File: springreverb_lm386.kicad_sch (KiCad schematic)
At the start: 67 parts, among them J1 IN, J10 VR2_3, J11 VR_2_2, J12 VR_2GND, J13 To, J14 FromSW, J15 To_Tank, J16 From_Tank, J17 FromGND, J18 From, J19 VR3_3, J2 INGND, J20 VR_4_3, J21 VR4_1, J22 OUT, J3 GND, J4 Vin, J5 LEDGND, J6 VR1_3, J7 toC6, J8 toC7, J9 FromC, SW1 SW_SPDT, SW2 SW_SPST, U1 TL072, U2 TC1044S, U3 LM386

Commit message: 接続の名称を変更
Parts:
- J9: value FromC -> FromC1
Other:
- moved on the sheet: J9
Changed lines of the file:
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@@
+	)
+	(junction
+		(at 39.37 140.97)
+		(diameter 0)
+		(color 0 0 0 0)
 	)
 	(junction
@@
 	)
 	(junction
-		(at 97.79 162.56)
-		(diameter 0)
-		(color 0 0 0 0)
-	)
-	(junction
 		(at 58.42 68.58)
 		(diameter 0)
@@
 	(wire
 		(pts
-			(xy 71.12 162.56) (xy 97.79 162.56)
+			(xy 71.12 162.56) (xy 105.41 162.56)
 		)
 		(stroke
@@
 	(wire
 		(pts
+			(xy 39.37 140.97) (xy 43.18 140.97)
+		)
+		(stroke
+			(width 0)
+			(type default)
+		)
+	)
+	(wire
+		(pts
 			(xy 60.96 68.58) (xy 58.42 68.58)
 		)
@@
 	(wire
 		(pts
-			(xy 26.67 140.97) (xy 43.18 140.97)
+			(xy 26.67 140.97) (xy 39.37 140.97)
 		)
 		(stroke
@@
 		(pts
 			(xy 165.1 143.51) (xy 165.1 144.78)
-		)
-		(stroke
-			(width 0)
-			(type default)
-		)
-	)
-	(wire
-		(pts
-			(xy 97.79 162.56) (xy 105.41 162.56)
 		)
 		(stroke
@@
 	(symbol
 		(lib_id "Connector:Conn_01x01_Pin")
-		(at 97.79 157.48 270)
+		(at 39.37 146.05 90)
 		(unit 1)
 		(body_style 1)
@@
 		(in_pos_files yes)
 		(dnp no)
-		(fields_autoplaced yes)
 		(property "Reference" "J9"
-			(at 99.06 156.8449 90)
+			(at 38.1 146.6851 90)
 			(show_name no)
 			(do_not_autoplace no)
@@
 			)
 		)
-		(property "Value" "FromC"
-			(at 99.06 159.3849 90)
+		(property "Value" "FromC1"
+			(at 38.1 144.272 90)
 			(show_name no)
 			(do_not_autoplace no)
@@
 		)
 		(property "Footprint" "MyLibrary:PinHeader_1x01_P2.54mm_Vertical"
-			(at 97.79 157.48 0)
+			(at 39.37 146.05 0)
 			(hide yes)
 			(show_name no)
@@
 		)
 		(property "Datasheet" ""
-			(at 97.79 157.48 0)
+			(at 39.37 146.05 0)
 			(hide yes)
 			(show_name no)
@@
 		)
 		(property "Description" "Generic connector, single row, 01x01, script generated"
-			(at 97.79 157.48 0)
+			(at 39.37 146.05 0)
 			(hide yes)
 			(show_name no)

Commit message: 不要な配線を修正
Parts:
- removed J12: VR_2GND, MyLibrary:PinHeader_1x01_P2.54mm_Vertical, symbol Connector:Conn_01x01_Pin
- J9: value FromC1 -> VR_1_1
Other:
- moved on the sheet: J9
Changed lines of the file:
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@@
-	)
-	(junction
-		(at 39.37 140.97)
-		(diameter 0)
-		(color 0 0 0 0)
 	)
 	(junction
@@
 	)
 	(junction
-		(at 124.46 162.56)
-		(diameter 0)
-		(color 0 0 0 0)
-	)
-	(junction
 		(at 166.37 34.29)
 		(diameter 0)
@@
 	)
 	(junction
+		(at 76.2 162.56)
+		(diameter 0)
+		(color 0 0 0 0)
+	)
+	(junction
 		(at 58.42 91.44)
 		(diameter 0)
@@
 	(wire
 		(pts
+			(xy 76.2 162.56) (xy 105.41 162.56)
+		)
+		(stroke
+			(width 0)
+			(type default)
+		)
+	)
+	(wire
+		(pts
 			(xy 58.42 76.2) (xy 58.42 82.55)
 		)
@@
 	(wire
 		(pts
-			(xy 124.46 162.56) (xy 134.62 162.56)
-		)
-		(stroke
-			(width 0)
-			(type default)
-		)
-	)
-	(wire
-		(pts
 			(xy 146.05 34.29) (xy 152.4 34.29)
 		)
@@
 	(wire
 		(pts
-			(xy 71.12 162.56) (xy 105.41 162.56)
+			(xy 71.12 162.56) (xy 76.2 162.56)
 		)
 		(stroke
@@
 	(wire
 		(pts
-			(xy 39.37 140.97) (xy 43.18 140.97)
-		)
-		(stroke
-			(width 0)
-			(type default)
-		)
-	)
-	(wire
-		(pts
 			(xy 60.96 68.58) (xy 58.42 68.58)
 		)
@@
 	(wire
 		(pts
-			(xy 26.67 140.97) (xy 39.37 140.97)
+			(xy 26.67 140.97) (xy 43.18 140.97)
 		)
 		(stroke
@@
 	(wire
 		(pts
-			(xy 110.49 162.56) (xy 124.46 162.56)
+			(xy 110.49 162.56) (xy 134.62 162.56)
 		)
 		(stroke
@@
 	(symbol
 		(lib_id "Connector:Conn_01x01_Pin")
-		(at 39.37 146.05 90)
+		(at 76.2 157.48 270)
 		(unit 1)
 		(body_style 1)
@@
 		(dnp no)
 		(property "Reference" "J9"
-			(at 38.1 146.6851 90)
+			(at 77.47 156.8449 90)
 			(show_name no)
 			(do_not_autoplace no)
@@
 			)
 		)
-		(property "Value" "FromC1"
-			(at 38.1 144.272 90)
+		(property "Value" "VR_1_1"
+			(at 77.47 159.258 90)
 			(show_name no)
 			(do_not_autoplace no)
@@
 		)
 		(property "Footprint" "MyLibrary:PinHeader_1x01_P2.54mm_Vertical"
-			(at 39.37 146.05 0)
+			(at 76.2 157.48 0)
 			(hide yes)
 			(show_name no)
@@
 		)
 		(property "Datasheet" ""
-			(at 39.37 146.05 0)
+			(at 76.2 157.48 0)
 			(hide yes)
 			(show_name no)
@@
 		)
 		(property "Description" "Generic connector, single row, 01x01, script generated"
-			(at 39.37 146.05 0)
+			(at 76.2 157.48 0)
 			(hide yes)
 			(show_name no)
@@
 					(unit 1)
 				)
-			)
-		)
-	)
-	(symbol
-		(lib_id "Connector:Conn_01x01_Pin")
-		(at 124.46 157.48 90)
-		(mirror x)
-		(unit 1)
-		(body_style 1)
-		(exclude_from_sim no)
-		(in_bom yes)
-		(on_board yes)
-		(in_pos_files yes)
-		(dnp no)
-		(property "Reference" "J12"
-			(at 129.54 156.718 90)
-			(show_name no)
-			(do_not_autoplace no)
-			(effects
-				(font
-					(size 1.27 1.27)
-				)
-				(justify left)
-			)
-		)
-		(property "Value" "VR_2GND"
-			(at 132.842 159.512 90)
-			(show_name no)
-			(do_not_autoplace no)
-			(effects
-				(font
-					(size 1.27 1.27)
-				)
-				(justify left)
-			)
-		)
-		(property "Footprint" "MyLibrary:PinHeader_1x01_P2.54mm_Vertical"
-			(at 124.46 157.48 0)
-			(hide yes)
-			(show_name no)
-			(do_not_autoplace no)
-			(effects
-				(font
-					(size 1.27 1.27)
-				)
-			)
-		)
-		(property "Datasheet" ""
-			(at 124.46 157.48 0)
-			(hide yes)
-			(show_name no)
-			(do_not_autoplace no)
-			(effects
-				(font
-					(size 1.27 1.27)
-				)
-			)
-		)
-		(property "Description" "Generic connector, single row, 01x01, script generated"
-			(at 124.46 157.48 0)
-			(hide yes)
-			(show_name no)
-			(do_not_autoplace no)
-			(effects
-				(font
-					(size 1.27 1.27)
-				)
-			)
-		)
-		(pin "1"
-		)
-		(instances
-			(project "springreverb_lm386"
-				(path "/db334565-2b42-4a43-9204-0bb0e555e376"
-					(reference "J12")
-					(unit 1)
-				)

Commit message: トーンのVRとコンデンサの値修整
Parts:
- C20: value 4700p -> 0.47u
- VR3: value A100k -> B10k
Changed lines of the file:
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@@
 			)
 		)
-		(property "Value" "A100k"
+		(property "Value" "B10k"
 			(at 215.9 154.94 0)
 			(show_name no)
@@
 			)
 		)
-		(property "Value" "4700p"
+		(property "Value" "0.47u"
 			(at 226.822 148.336 0)
 			(show_name no)

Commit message: LM386に向かうCの値を変更
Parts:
- C6: value 0.1u -> 0.047u
- VR3: value B10k -> B5k
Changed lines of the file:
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@@
 			)
 		)
-		(property "Value" "0.1u"
+		(property "Value" "0.047u"
 			(at 100.838 144.272 90)
 			(show_name no)
@@
 			)
 		)
-		(property "Value" "B10k"
+		(property "Value" "B5k"
 			(at 215.9 154.94 0)
 			(show_name no)

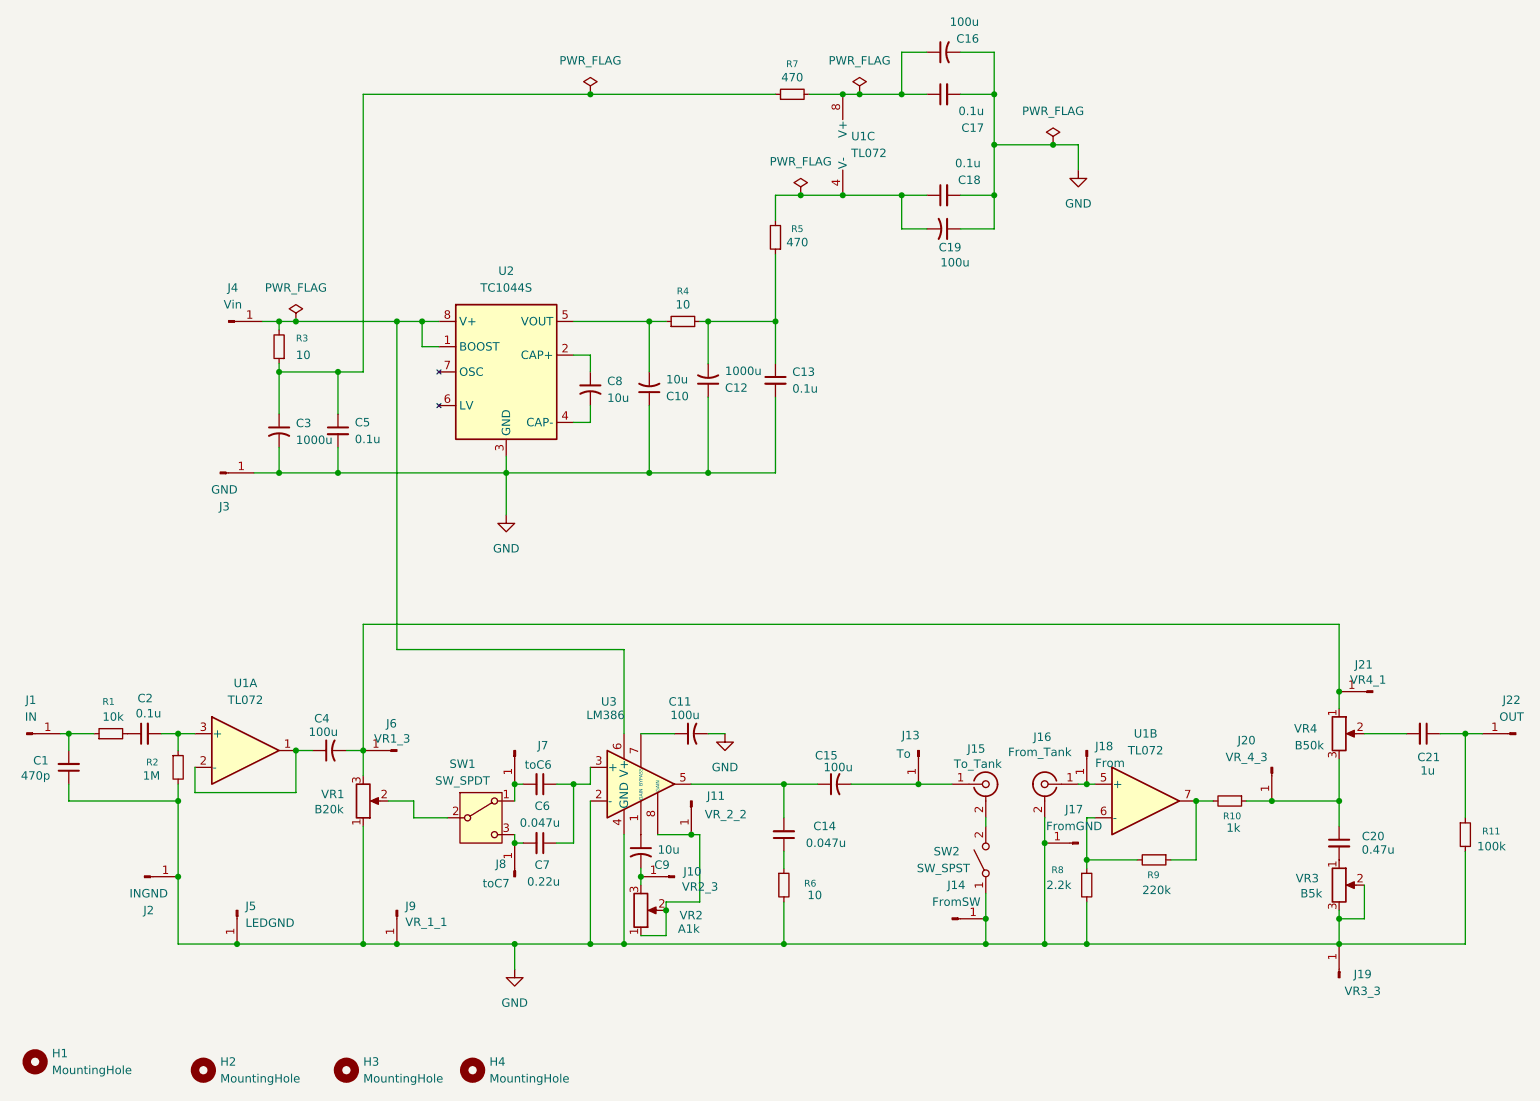
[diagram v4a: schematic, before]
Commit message: dryをできるだけ原音のままにするため3番ピンから取り出し。 トーンVRで無音になる問題を修正。
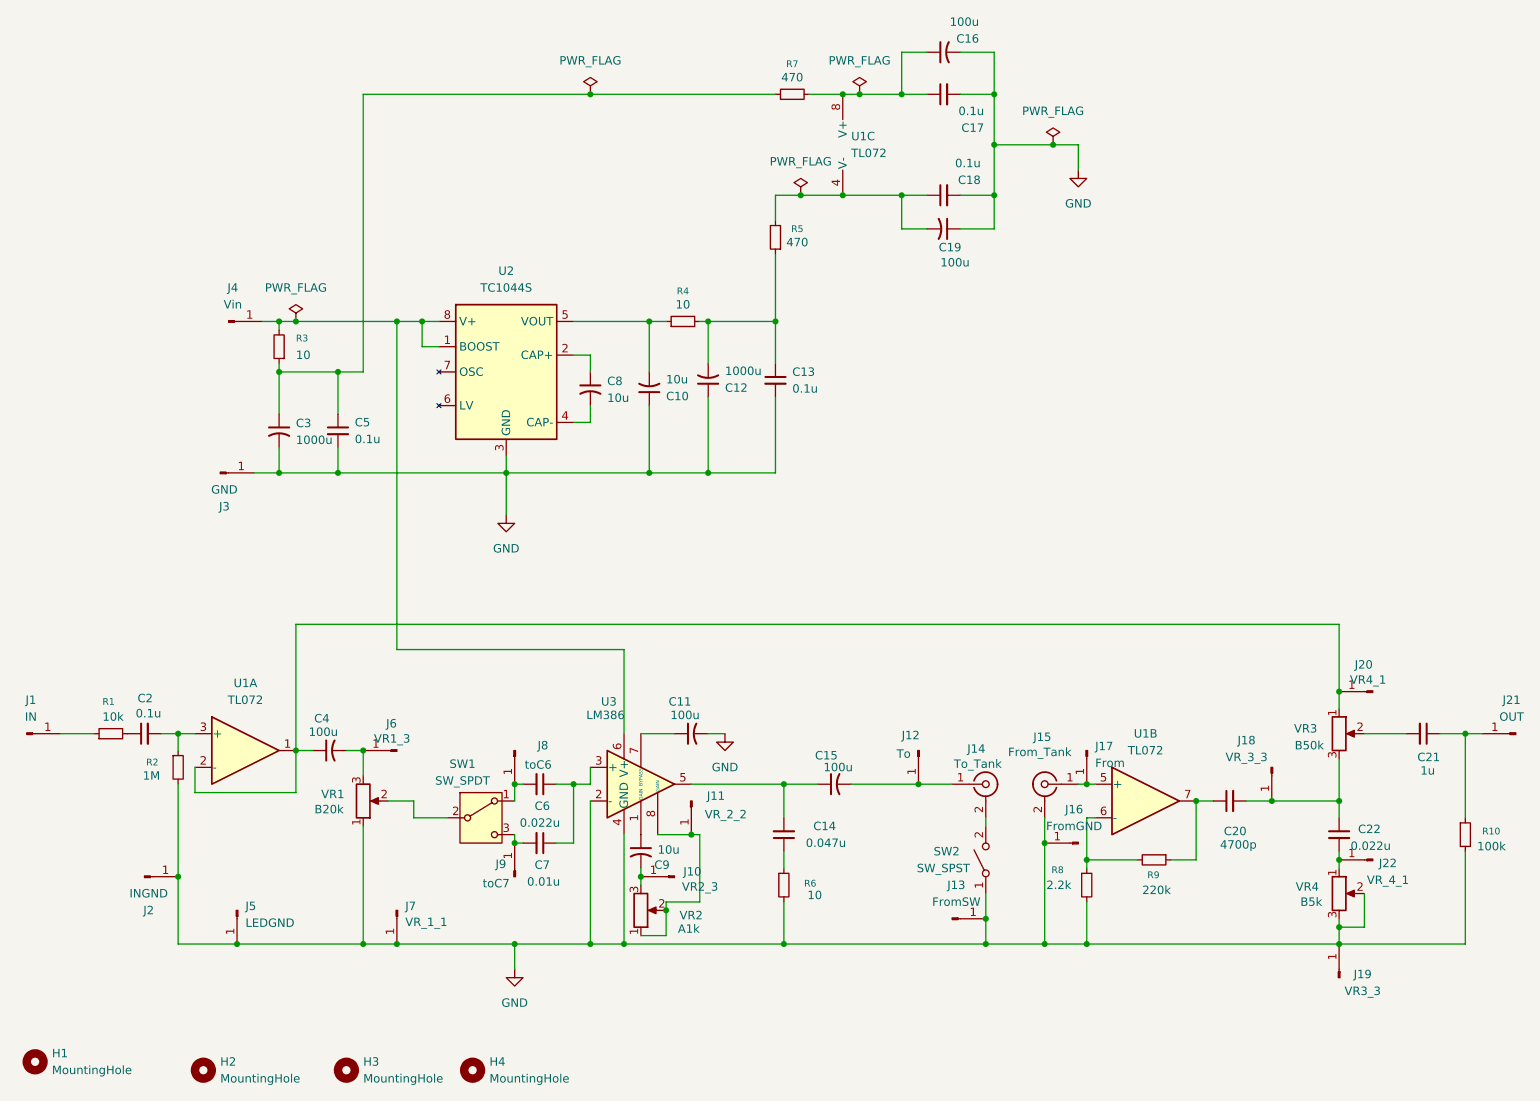
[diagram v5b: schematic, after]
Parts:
- removed C1: 470p, symbol Device:C_Small
- removed R10: 1k, Resistor_THT:R_Axial_DIN0204_L3.6mm_D1.6mm_P7.62mm_Horizontal, symbol Device:R_Small
- added C22: 0.022u, MyLibrary:9.3_4.3_p7.5, symbol Device:C_Small
- added J22: VR_4_1, MyLibrary:PinHeader_1x01_P2.54mm_Vertical, symbol Connector:Conn_01x01_Pin
- C20: value 0.47u -> 4700p; footprint (none) -> MyLibrary:9.3_4.3_p7.5
- C6: value 0.047u -> 0.022u
- C7: value 0.22u -> 0.01u; footprint MyLibrary:11.2_4.3_p10 -> MyLibrary:9.3_4.3_p7.5
- J18: renamed from J20; value VR_4_3 -> VR_3_3
- renumbered J13 to J12, J14 to J13, J15 to J14, J16 to J15, J17 to J16, J18 to J17, J21 to J20, J22 to J21, J9 to J7, J7 to J8, J8 to J9, R11 to R10, VR4 to VR3, VR3 to VR4
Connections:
- net at J18.1 (Pin_1), VR3.3: now also C20.2, C22.1; no longer C20.1
- net at C4.2, J6.1 (Pin_1), VR1.3: no longer J20.1 (Pin_1), VR3.1
- net at R9.1, U1.7: now also C20.1
- net at C4.1, U1.1, U1.2 (-): now also J20.1 (Pin_1), VR3.1
- net at VR4.1: now also C22.2, J22.1 (Pin_1); no longer C20.2
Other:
- moved on the sheet: VR4

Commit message: トーン回路周りを修正
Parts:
- removed C22: 0.022u, MyLibrary:9.3_4.3_p7.5, symbol Device:C_Small
- removed J22: VR_4_1, MyLibrary:PinHeader_1x01_P2.54mm_Vertical, symbol Connector:Conn_01x01_Pin
- C20: value 4700p -> 0.022uF
- J18: value VR_3_3 -> VR_4_1
- J19: value VR3_3 -> VR4_3
- J20: value VR4_1 -> VR3_1
- VR4: value B5k -> B20k
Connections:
- net GND: now also VR3.3
- net at C20.2, J18.1 (Pin_1): now also VR4.1; no longer VR3.3
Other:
- moved on the sheet: J18, J19, VR3, VR4

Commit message: トーン回路の修正
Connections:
- net GND: no longer VR3.3
- net at C20.2, J18.1 (Pin_1), VR4.1: now also VR3.3
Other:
- moved on the sheet: J20, VR3
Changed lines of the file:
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@@
 	)
 	(junction
-		(at 218.44 151.13)
+		(at 105.41 162.56)
 		(diameter 0)
 		(color 0 0 0 0)
 	)
 	(junction
-		(at 105.41 162.56)
+		(at 173.99 147.32)
 		(diameter 0)
 		(color 0 0 0 0)
 	)
 	(junction
-		(at 173.99 147.32)
+		(at 213.36 140.97)
 		(diameter 0)
 		(color 0 0 0 0)
@@
 	)
 	(junction
-		(at 218.44 124.46)
+		(at 116.84 157.48)
 		(diameter 0)
 		(color 0 0 0 0)
 	)
 	(junction
-		(at 116.84 157.48)
+		(at 76.2 68.58)
 		(diameter 0)
 		(color 0 0 0 0)
 	)
 	(junction
-		(at 76.2 68.58)
+		(at 166.37 34.29)
 		(diameter 0)
 		(color 0 0 0 0)
 	)
 	(junction
-		(at 166.37 34.29)
+		(at 213.36 124.46)
 		(diameter 0)
 		(color 0 0 0 0)
@@
 	(wire
 		(pts
-			(xy 218.44 151.13) (xy 223.52 151.13)
-		)
-		(stroke
-			(width 0)
-			(type default)
-		)
-	)
-	(wire
-		(pts
 			(xy 116.84 157.48) (xy 116.84 161.29)
 		)
@@
 	(wire
 		(pts
-			(xy 218.44 125.73) (xy 218.44 124.46)
-		)
-		(stroke
-			(width 0)
-			(type default)
-		)
-	)
-	(wire
-		(pts
 			(xy 71.12 76.2) (xy 71.12 34.29)
 		)
@@
 	(wire
 		(pts
-			(xy 223.52 125.73) (xy 218.44 125.73)
-		)
-		(stroke
-			(width 0)
-			(type default)
-		)
-	)
-	(wire
-		(pts
 			(xy 133.35 58.42) (xy 133.35 68.58)
 		)
@@
 	(wire
 		(pts
-			(xy 227.33 130.81) (xy 228.6 130.81)
+			(xy 217.17 130.81) (xy 228.6 130.81)
 		)
 		(stroke
@@
 	(wire
 		(pts
-			(xy 60.96 114.3) (xy 218.44 114.3)
+			(xy 60.96 114.3) (xy 213.36 114.3)
 		)
 		(stroke
@@
 	(wire
 		(pts
-			(xy 218.44 114.3) (xy 218.44 124.46)
-		)
-		(stroke
-			(width 0)
-			(type default)
-		)
-	)
-	(wire
-		(pts
 			(xy 166.37 54.61) (xy 161.29 54.61)
 		)
@@
 	(wire
 		(pts
-			(xy 223.52 125.73) (xy 223.52 127)
+			(xy 213.36 114.3) (xy 213.36 124.46)
 		)
 		(stroke
@@
 	(wire
 		(pts
+			(xy 213.36 124.46) (xy 213.36 127)
+		)
+		(stroke
+			(width 0)
+			(type default)
+		)
+	)
+	(wire
+		(pts
 			(xy 133.35 80.01) (xy 133.35 91.44)
 		)
@@
 	(wire
 		(pts
-			(xy 223.52 151.13) (xy 223.52 134.62)
+			(xy 213.36 134.62) (xy 213.36 140.97)
 		)
 		(stroke
@@
 	(symbol
 		(lib_id "Connector:Conn_01x01_Pin")
-		(at 223.52 124.46 180)
+		(at 218.44 124.46 180)
 		(unit 1)
 		(body_style 1)
@@
 		(dnp no)
 		(property "Reference" "J20"
-			(at 223.52 120.396 0)
+			(at 218.44 120.396 0)
 			(show_name no)
 			(do_not_autoplace no)
@@
 		)
 		(property "Value" "VR3_1"
-			(at 225.552 122.682 0)
+			(at 220.472 122.682 0)
 			(show_name no)
 			(do_not_autoplace no)
@@
 		)
 		(property "Footprint" "MyLibrary:PinHeader_1x01_P2.54mm_Vertical"
-			(at 223.52 124.46 0)
+			(at 218.44 124.46 0)
 			(hide yes)
 			(show_name no)
@@
 		)
 		(property "Datasheet" ""
-			(at 223.52 124.46 0)
+			(at 218.44 124.46 0)
 			(hide yes)
 			(show_name no)
@@
 		)
 		(property "Description" "Generic connector, single row, 01x01, script generated"
-			(at 223.52 124.46 0)
+			(at 218.44 124.46 0)
 			(hide yes)
 			(show_name no)
@@
 	(symbol
 		(lib_id "Device:R_Potentiometer")
-		(at 223.52 130.81 0)
+		(at 213.36 130.81 0)
 		(unit 1)
 		(body_style 1)
@@
 		(dnp no)
 		(property "Reference" "VR3"
-			(at 220.218 130.048 0)
+			(at 210.058 130.048 0)
 			(show_name no)
 			(do_not_autoplace no)
@@
 		)
 		(property "Value" "B50k"
-			(at 221.234 132.588 0)
+			(at 211.074 132.588 0)
 			(show_name no)
 			(do_not_autoplace no)
@@
 		)
 		(property "Footprint" ""
-			(at 223.52 130.81 0)
+			(at 213.36 130.81 0)
 			(hide yes)
 			(show_name no)
@@
 		)
 		(property "Datasheet" ""
-			(at 223.52 130.81 0)
+			(at 213.36 130.81 0)
 			(hide yes)
 			(show_name no)
@@
 		)
 		(property "Description" "Potentiometer"
-			(at 223.52 130.81 0)
+			(at 213.36 130.81 0)
 			(hide yes)
 			(show_name no)
